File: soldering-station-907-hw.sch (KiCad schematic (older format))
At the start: 37 parts, among them J1 DC in, J2 handle, Q1 IRFZ44N, Q2 PN2222A, Q3 PN2907A, Q4 PN2222A, SW1 PEC11R-4220F-S0024, U1 LM2596_regulator_module, U2 MCP602

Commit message: Parts placed.
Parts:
- A1: Comments This is a lie: Mount on 2x Sullins PPPC201LFBN-RC -> Mount on 2x Sullins PPPC151LFBN-RC
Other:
- note added: "C5 might be redundant."
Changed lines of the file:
@@
 encoding utf-8
 Sheet 1 1
-Title "Soldering station 907"
+Title "Soldering Station 907"
 Date "2019-07-24"
 Rev "v0.0.1"
@@
 F 3 "https://store.arduino.cc/usa/arduino-nano" H 10000 3350 50  0001 C CNN
 F 4 "Any Arduino Nano v3.x" H 10000 4350 50  0001 C CNN "P/N"
-F 5 "This is a lie: Mount on 2x Sullins PPPC201LFBN-RC" H 10000 4350 50  0001 C CNN "Comments"
+F 5 "Mount on 2x Sullins PPPC151LFBN-RC" H 10000 4350 50  0001 C CNN "Comments"
 	1    10000 4350
 	1    0    0    -1
@@
 Text Notes 2100 2400 0    50   ~ 0
 To 24VDC, 3A supply.
+Text Notes 10500 2950 0    50   ~ 0
+C5 might be redundant.
 $EndSCHEMATC

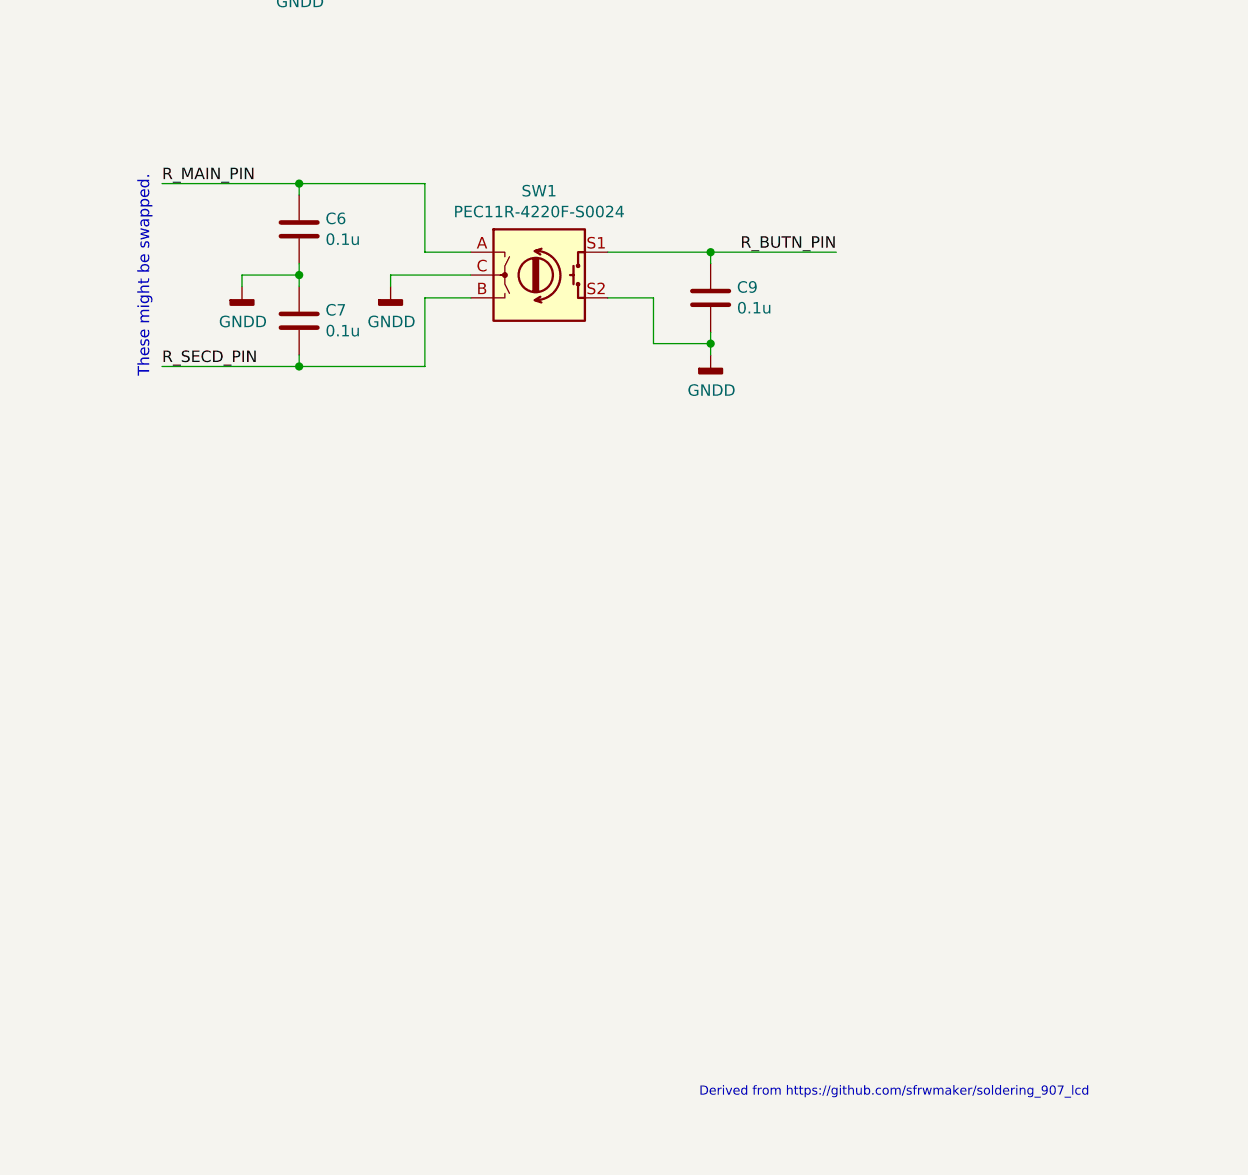
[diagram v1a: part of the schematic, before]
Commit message: Swapped R/L pins of SW1. Moved RV1 to front of board. Routing tweaks.
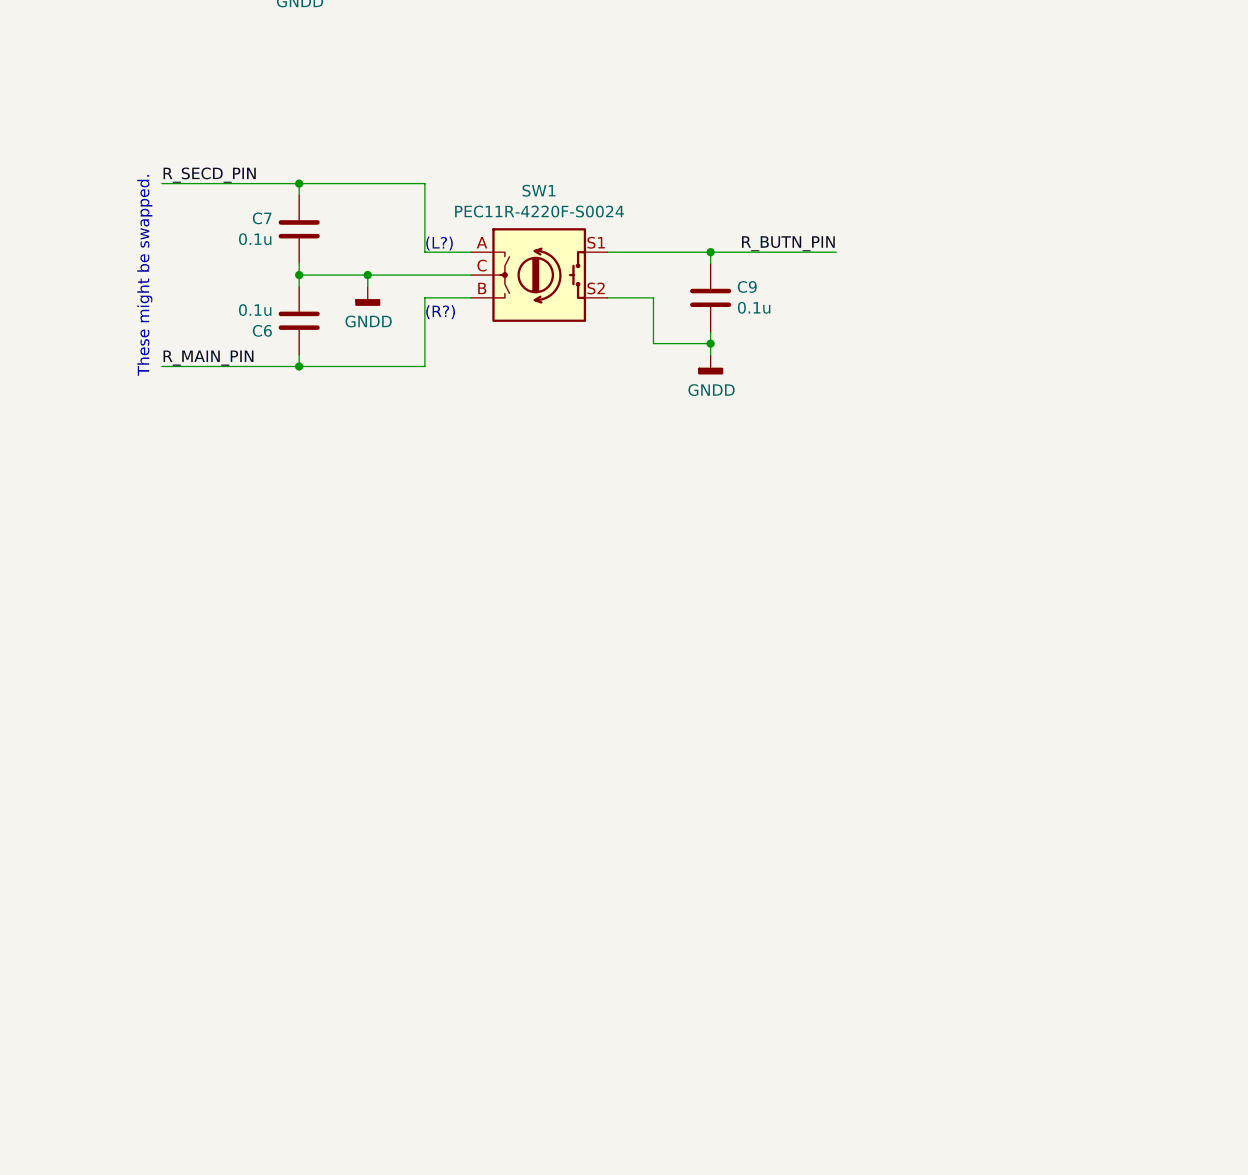
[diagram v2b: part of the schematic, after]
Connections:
- net GNDD: now also C7.2; no longer C7.1
- net R_MAIN_PIN: now also SW1.B; no longer SW1.A
- net R_SECD_PIN: now also C7.1, SW1.A; no longer C7.2, SW1.B
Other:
- note added: "(L?)"
- note added: "(R?)"
- note removed: "Derived from https://github.com/sfrwmaker/soldering_907_lcd"
- moved on the sheet: C6, C7
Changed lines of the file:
@@
 Sheet 1 1
 Title "Soldering Station 907"
-Date "2019-07-24"
+Date "2019-07-25"
 Rev "v0.0.1"
 Comp "Mithat Konar"
 Comment1 ""
 Comment2 ""
-Comment3 ""
-Comment4 ""
+Comment3 "derived from https://github.com/sfrwmaker/soldering_907_lcd"
+Comment4 "https://github.com/mithat/soldering-station-907-hw"
 $EndDescr
-Text Notes 14550 10100 0    40   ~ 0
-Derived from https://github.com/sfrwmaker/soldering_907_lcd
 $Comp
 L local:Arduino_Nano_v3.x A1
@@
 L power:GNDD #PWR025
 U 1 1 5D374F69
-P 13200 6550
-F 0 "#PWR025" H 13200 6300 50  0001 C CNN
-F 1 "GNDD" H 13204 6395 50  0000 C CNN
-F 2 "" H 13200 6550 50  0001 C CNN
-F 3 "" H 13200 6550 50  0001 C CNN
-	1    13200 6550
+P 13100 6550
+F 0 "#PWR025" H 13100 6300 50  0001 C CNN
+F 1 "GNDD" H 13104 6395 50  0000 C CNN
+F 2 "" H 13100 6550 50  0001 C CNN
+F 3 "" H 13100 6550 50  0001 C CNN
+	1    13100 6550
 	1    0    0    -1
 $EndComp
@@
 	13350 6600 13550 6600
 Wire Wire Line
-	13550 6500 13200 6500
-Wire Wire Line
-	13200 6500 13200 6550
+	13550 6500 13100 6500
+Wire Wire Line
+	13100 6500 13100 6550
 $Comp
 L Device:C C6
 U 1 1 5D377544
+P 12800 6700
+F 0 "C6" H 12915 6746 50  0000 L CNN
+F 1 "0.1u" H 12915 6655 50  0000 L CNN
+F 2 "Capacitor_THT:C_Rect_L4.0mm_W2.5mm_P2.50mm" H 12838 6550 50  0001 C CNN
+F 3 "" H 12800 6700 50  0001 C CNN
+F 4 "Vishay  K104K15X7RF5TL2" H 12800 6700 50  0001 C CNN "P/N"
+	1    12800 6700
+	-1   0    0    1
+$EndComp
+Wire Wire Line
+	12800 6150 12800 6100
+$Comp
+L Device:C C7
+U 1 1 5D377B4E
 P 12800 6300
-F 0 "C6" H 12915 6346 50  0000 L CNN
+F 0 "C7" H 12915 6346 50  0000 L CNN
 F 1 "0.1u" H 12915 6255 50  0000 L CNN
 F 2 "Capacitor_THT:C_Rect_L4.0mm_W2.5mm_P2.50mm" H 12838 6150 50  0001 C CNN
@@
 F 4 "Vishay  K104K15X7RF5TL2" H 12800 6300 50  0001 C CNN "P/N"
 	1    12800 6300
-	1    0    0    -1
-$EndComp
-Wire Wire Line
-	12800 6150 12800 6100
-$Comp
-L power:GNDD #PWR022
-U 1 1 5D3777F5
-P 12550 6550
-F 0 "#PWR022" H 12550 6300 50  0001 C CNN
-F 1 "GNDD" H 12554 6395 50  0000 C CNN
-F 2 "" H 12550 6550 50  0001 C CNN
-F 3 "" H 12550 6550 50  0001 C CNN
-	1    12550 6550
-	1    0    0    -1
-$EndComp
-Wire Wire Line
-	12800 6450 12800 6500
-Wire Wire Line
-	12800 6500 12550 6500
-Wire Wire Line
-	12550 6500 12550 6550
-$Comp
-L Device:C C7
-U 1 1 5D377B4E
-P 12800 6700
-F 0 "C7" H 12915 6746 50  0000 L CNN
-F 1 "0.1u" H 12915 6655 50  0000 L CNN
-F 2 "Capacitor_THT:C_Rect_L4.0mm_W2.5mm_P2.50mm" H 12838 6550 50  0001 C CNN
-F 3 "" H 12800 6700 50  0001 C CNN
-F 4 "Vishay  K104K15X7RF5TL2" H 12800 6700 50  0001 C CNN "P/N"
-	1    12800 6700
-	1    0    0    -1
-$EndComp
-Wire Wire Line
-	12800 6550 12800 6500
-Connection ~ 12800 6500
+	-1   0    0    -1
+$EndComp
 Wire Wire Line
 	12800 6850 12800 6900
@@
 Wire Wire Line
 	14600 6850 14600 6800
+Text Label 12200 6100 0    50   ~ 0
+R_SECD_PIN
 Text Label 12200 6900 0    50   ~ 0
-R_SECD_PIN
-Text Label 12200 6100 0    50   ~ 0
 R_MAIN_PIN
 Wire Wire Line
@@
 Text Notes 10500 2950 0    50   ~ 0
 C5 might be redundant.
+Text Notes 13350 6700 0    50   ~ 0
+(R?)
+Text Notes 13350 6400 0    50   ~ 0
+(L?)
+Wire Wire Line
+	12800 6450 12800 6500
+Wire Wire Line
+	13100 6500 12800 6500
+Connection ~ 13100 6500
+Connection ~ 12800 6500
+Wire Wire Line
+	12800 6500 12800 6550
 $EndSCHEMATC
